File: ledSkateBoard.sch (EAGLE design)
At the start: 25 parts, among them J1 JST, U1 MPU-9150, U2 ATMEGA328P_TQFP, U4 MIC2505 3.3

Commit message: Final on revA
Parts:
- removed R10: 36K, SparkFun-Resistors:RESISTOR0805-RES
- removed R9: 4.3K, SparkFun-Resistors:RESISTOR0805-RES
- removed TP3: TEST-POINT3, SparkFun-Passives:TEST-POINT3
- added C2, C3: 22pF, SparkFun-Capacitors:CAP1206
- added C4: 10uF, SparkFun-Capacitors:CAP1206
- added D2: GREEN, SparkFun-LED:LED-GREENLARGE
- added D3, D4: PMEG4005EJ, SparkFun-DiscreteSemi:DIODE-SCHOTTKY-PMEG4005EJ
- added FB1: (no value), microbuilder:FERRITE0805
- added JP2: (no value), SparkFun-Connectors:M06LOCK
- added Q1: 16Mhz, adafruit:CRYSTALHC49S
- added R1: 330, SparkFun-Passives:RESISTOR1206
- added R2: 37K, SparkFun-Passives:RESISTOR1206
- added R3: 430K, SparkFun-Passives:RESISTOR1206
- added U3: (no value), adafruit:GPS_FGPMMOPA6H
- C1: value 10uF -> 10nF; device SparkFun-Capacitors:CAP0805 -> SparkFun-Capacitors:CAP1206
- C10, C13, C14, C15, C17, C9: device SparkFun-Capacitors:CAP0805 -> SparkFun-Capacitors:CAP1206
- C11: value 4.7uF -> .1uF; device SparkFun-Capacitors:CAP0805 -> SparkFun-Capacitors:CAP1206
- C12: value 4.7uF -> 2.2nF 50V; device SparkFun-Capacitors:CAP0805 -> SparkFun-Capacitors:CAP1206
- D1: device SparkFun-LED:LED-RED0603 -> SparkFun-LED:LED-RED1206
- JP3: value LED CONNECTOR -> M02LOCK; device SparkFun-Connectors:M03PTH -> SparkFun-Connectors:M02LOCK
- R11, R12: value 10K -> 4.7K; device SparkFun-Resistors:RESISTOR0805-RES -> SparkFun-Passives:RESISTOR1206
- R13, R14, R8: device SparkFun-Resistors:RESISTOR0805-RES -> SparkFun-Passives:RESISTOR1206
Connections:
- removed net DATA: JP3.2, U2.PB0(ICP)
- removed net MPU_INT: U1.INT, U2.PD2(INT0)
- new net AN0: JP2.2, U2.PD6(AIN0)
- new net AN1: JP2.3, U2.PD7(AIN1)
- new net GPS_RX: JP3.2, U2.PD1(TXD), U3.RX
- new net GPS_TX: JP3.1, U2.PD0(RXD), U3.TX
- new net N$10: C14.2, D3.C, D4.C, U4.EN, U4.IN
- new net N$3: C2.1, Q1.2, U2.PB6(XTAL1/TOSC1)
- new net N$5: C3.1, Q1.1, U2.PB7(XTAL2/TOSC2)
- new net N$6: D2.A, U3.3D-FIX
- new net N$9: D2.C, R1.1
- new net PB0: JP2.4
- new net PB1: JP2.5, U2.PB1(OC1A)
- new net PB2: JP2.6, U2.PB2(SS/OC1B)
- new net PD5: JP2.1, U2.PD5(T1)
- new net PWR_MNTR: R2.1, R3.2, U2.PC0(ADC0)
- net 5V: now also D3.A, JP1.2
- net GND: now also C2.2, C3.2, C4.2, R1.2, R3.1, U3.GND@1, U3.GND@2, U3.GND@4; no longer JP3.3, R10.1
- net N$4: now also C4.1, FB1.P$1, U3.VCC; no longer R10.2, R9.1, TP3.1, U2.PC0(ADC0)
- net VCC: now also FB1.P$2; no longer JP1.2
- net V_BATT: now also D4.A, R2.2; no longer C14.2, JP3.1, R9.2, U4.EN, U4.IN
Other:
- moved on the sheet: C1, C10, C11, C12, C13, C14, C15, C17, C9, D1, J1, JP1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

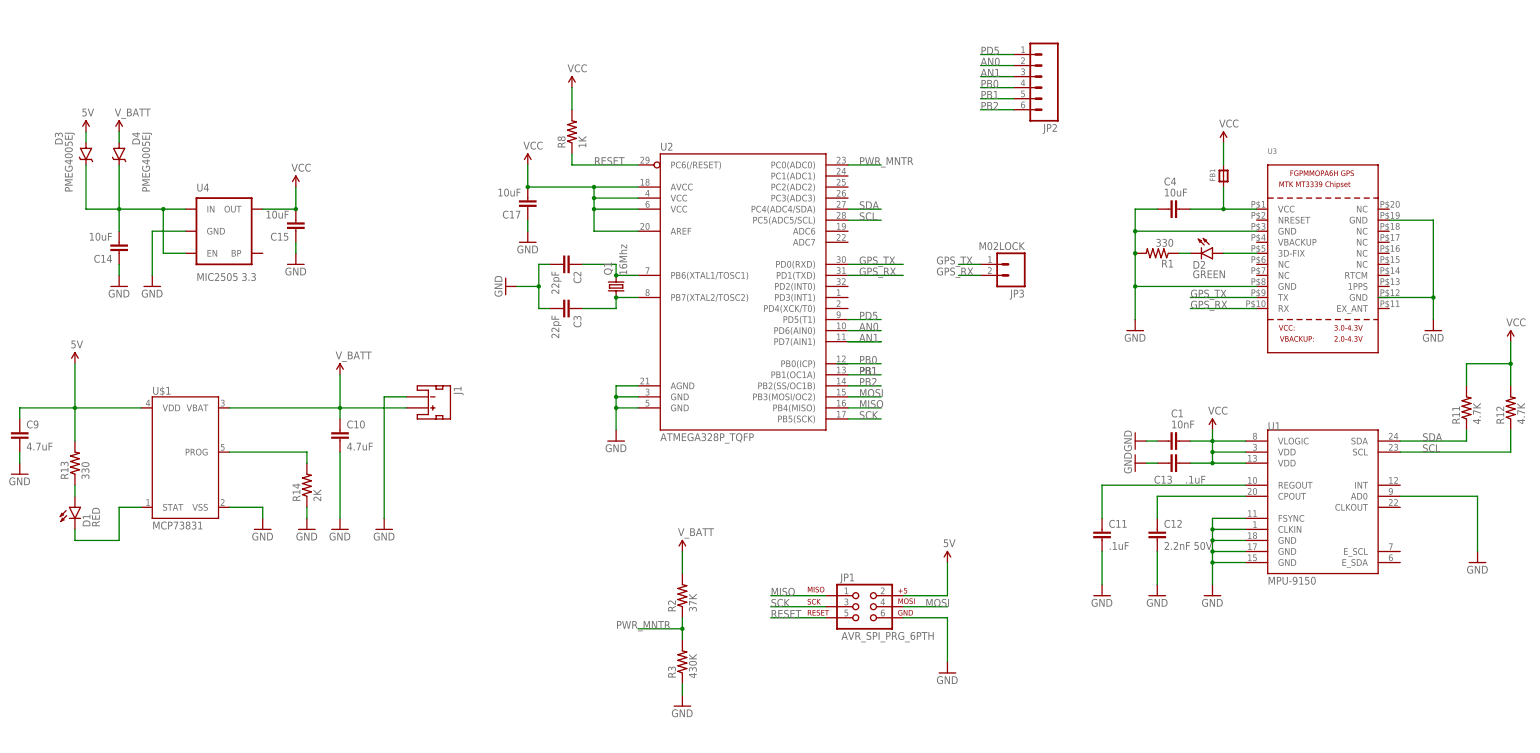
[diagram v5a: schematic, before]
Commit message: Changed to lpc1114 and BNO055
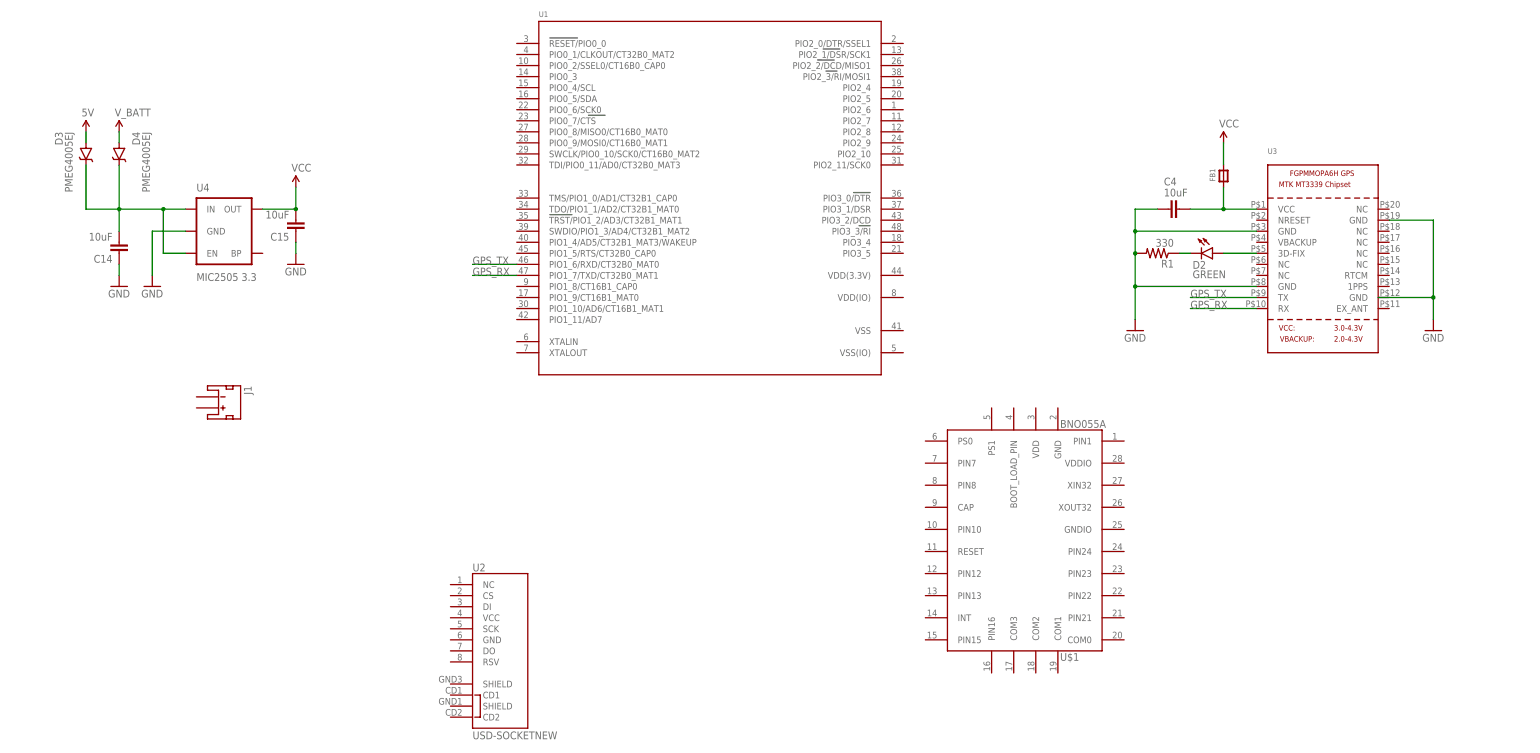
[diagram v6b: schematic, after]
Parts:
- removed C1: 10nF, SparkFun-Capacitors:CAP1206
- removed C10, C9: 4.7uF, SparkFun-Capacitors:CAP1206
- removed C11, C13: .1uF, SparkFun-Capacitors:CAP1206
- removed C12: 2.2nF 50V, SparkFun-Capacitors:CAP1206
- removed C17: 10uF, SparkFun-Capacitors:CAP1206
- removed C2, C3: 22pF, SparkFun-Capacitors:CAP1206
- removed D1: RED, SparkFun-LED:LED-RED1206
- removed JP1: AVR_SPI_PRG_6PTH, SparkFun-Connectors:AVR_SPI_PRG_6PTH
- removed JP2: (no value), SparkFun-Connectors:M06LOCK
- removed JP3: M02LOCK, SparkFun-Connectors:M02LOCK
- removed Q1: 16Mhz, adafruit:CRYSTALHC49S
- removed R11, R12: 4.7K, SparkFun-Passives:RESISTOR1206
- removed R13: 330, SparkFun-Passives:RESISTOR1206
- removed R14: 2K, SparkFun-Passives:RESISTOR1206
- removed R2: 37K, SparkFun-Passives:RESISTOR1206
- removed R3: 430K, SparkFun-Passives:RESISTOR1206
- removed R8: 1K, SparkFun-Passives:RESISTOR1206
- U$1: value MCP73831 -> BNO055A; device GeekAmmo:MCP73831 -> BNO055:BNO055A
- U1: value MPU-9150 -> (none); device SparkFun-Sensors:MPU-9150QFN-24-NP -> microbuilder:LPC1113/4
- U2: value ATMEGA328P_TQFP -> USD-SOCKETNEW; device SparkFun-DigitalIC:ATMEGA328P_TQFP -> SparkFun-Connectors:USD-SOCKETNEW
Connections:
- removed net AN0: JP2.2, U2.PD6(AIN0)
- removed net AN1: JP2.3, U2.PD7(AIN1)
- removed net MISO: JP1.1, U2.PB4(MISO)
- removed net MOSI: JP1.4, U2.PB3(MOSI/OC2)
- removed net N$1: C11.1, U1.REGOUT
- removed net N$11: R14.2, U$1.PROG
- removed net N$2: C12.1, U1.CPOUT
- removed net N$3: C2.1, Q1.2, U2.PB6(XTAL1/TOSC1)
- removed net N$5: C3.1, Q1.1, U2.PB7(XTAL2/TOSC2)
- removed net N$7: D1.A, R13.1
- removed net N$8: D1.C, U$1.STAT
- removed net PB0: JP2.4
- removed net PB1: JP2.5, U2.PB1(OC1A)
- removed net PB2: JP2.6, U2.PB2(SS/OC1B)
- removed net PD5: JP2.1, U2.PD5(T1)
- removed net PWR_MNTR: R2.1, R3.2, U2.PC0(ADC0)
- removed net RESET: JP1.5, R8.1, U2.PC6(/RESET)
- removed net SCK: JP1.3, U2.PB5(SCK)
- removed net SCL: R12.1, U1.SCL, U2.PC5(ADC5/SCL)
- removed net SDA: R11.1, U1.SDA, U2.PC4(ADC4/SDA)
- net 5V: no longer C9.1, JP1.2, R13.2, U$1.VDD
- net GND: no longer C1.1, C10.2, C11.2, C12.2, C13.1, C17.1, C2.2, C3.2, C9.2, J1.-, JP1.6, R14.1, R3.1, U$1.VSS, U1.AD0, U1.CLKIN, U1.FSYNC, U1.GND@15, U1.GND@17, U1.GND@18, U2.AGND, U2.GND@3, U2.GND@5
- net GPS_RX: now also U1.PIO1_7/TXD/CT32B0_MAT1; no longer JP3.2, U2.PD1(TXD)
- net GPS_TX: now also U1.PIO1_6/RXD/CT32B0_MAT0; no longer JP3.1, U2.PD0(RXD)
- net VCC: no longer C1.2, C13.2, C17.2, R11.2, R12.2, R8.2, U1.VDD@13, U1.VDD@3, U1.VLOGIC, U2.AREF, U2.AVCC, U2.VCC@4, U2.VCC@6
- net V_BATT: no longer C10.1, J1.+, R2.2, U$1.VBAT
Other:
- moved on the sheet: J1

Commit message: faileld attempt
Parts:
- removed D3, D4: PMEG4005EJ, SparkFun-DiscreteSemi:DIODE-SCHOTTKY-PMEG4005EJ
- removed U2: USD-SOCKETNEW, SparkFun-Connectors:USD-SOCKETNEW
- removed U3: (no value), adafruit:GPS_FGPMMOPA6H
- added BNO055: BNO055A, BNO055:BNO055A
- added BNO180: BMP180, SparkFun-Sensors:BMP180
- added C2, C3, C6, C7: 10uF, SparkFun-Passives:CAP0805
- added C5: .1uF, SparkFun-Passives:CAP0805
- added D1: PURPLE, SparkFun-LED:LED-PURPLE1206
- added ISP_SWITCH, RST_SWITCH: SWITCH-MOMENTARY-2SMD-1101NE, SparkFun-Electromechanical:SWITCH-MOMENTARY-2SMD-1101NE
- added JP1: (no value), SparkFun-Connectors:M04LOCK
- added MTK339: (no value), adafruit:GPS_FGPMMOPA6H
- added R2, R3, R5, R6: 10K, SparkFun-Passives:RESISTOR0805-RES
- added R4: 330, SparkFun-Passives:RESISTOR0805-RES
- C14, C15, C4: device SparkFun-Capacitors:CAP1206 -> SparkFun-Passives:CAP0805
- R1: device SparkFun-Passives:RESISTOR1206 -> SparkFun-Passives:RESISTOR0805-RES
- U$1: value BNO055A -> MICROSD; device BNO055:BNO055A -> adafruit:MICROSD
- renumbered U1 to LPC1114
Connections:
- removed net 5V: D3.A
- removed net GPS_RX: LPC1114.PIO1_7/TXD/CT32B0_MAT1, U3.RX
- removed net GPS_TX: LPC1114.PIO1_6/RXD/CT32B0_MAT0, U3.TX
- removed net N$10: C14.2, D3.C, D4.C, U4.EN, U4.IN
- new net BNO_INT: BNO055.INT, LPC1114.PIO0_3
- new net ISP: ISP_SWITCH.2, LPC1114.PIO0_1/CLKOUT/CT32B0_MAT2, R5.1
- new net LPC_RX: JP1.2, LPC1114.PIO1_6/RXD/CT32B0_MAT0, MTK339.TX
- new net LPC_TX: JP1.3, LPC1114.PIO1_7/TXD/CT32B0_MAT1, MTK339.RX
- new net N$1: D1.A, LPC1114.PIO2_6
- new net N$2: BNO055.CAP, C2.2
- new net N$3: D1.C, R4.2
- new net RESET: LPC1114.RESET/PIO0_0, R6.1, RST_SWITCH.2
- new net SCL: BNO055.COM1, BNO180.SCL, LPC1114.PIO0_4/SCL, R3.2
- new net SDA: BNO055.COM0, BNO180.SDA, LPC1114.PIO0_5/SDA, R2.2
- new net SD_CS: LPC1114.PIO0_2/SSEL0/CT16B0_CAP0, U$1.CS
- new net SD_DETECT: U$1.CARD_DETECT
- new net SD_DI: LPC1114.PIO0_9/MOSI0/CT16B0_MAT1, U$1.DATA_IN
- new net SD_DO: LPC1114.PIO0_8/MISO0/CT16B0_MAT0, U$1.DATA_OUT
- new net SD_SCK: LPC1114.PIO0_6/SCK0, U$1.SCLK
- new net VDD: U$1.VDD
- new net VSS: U$1.VSS
- net GND: now also BNO055.COM2, BNO055.COM3, BNO055.GND, BNO055.GNDIO, BNO055.PIN10, BNO055.PIN15, BNO055.PIN16, BNO055.PS0, BNO055.PS1, BNO180.GND, C2.1, C3.2, C5.1, C6.2, C7.2, ISP_SWITCH.1, J1.-, JP1.4, LPC1114.VSS, LPC1114.VSS(IO), MTK339.GND@1, MTK339.GND@2, MTK339.GND@3, MTK339.GND@4, R4.1, RST_SWITCH.1, U$1.GND, U$1.GND1; no longer U3.GND@1, U3.GND@2, U3.GND@4
- net N$4: now also MTK339.VCC; no longer U3.VCC
- net N$6: now also MTK339.3D-FIX; no longer U3.3D-FIX
- net VCC: now also BNO055.BOOT_LOAD_PIN, BNO055.RESET, BNO055.VDD, BNO055.VDDIO, BNO180.VDD, BNO180.VDDIO, C3.1, C5.2, C6.1, C7.1, JP1.1, LPC1114.VDD(3.3V), LPC1114.VDD(IO), R2.1, R3.1, R5.2, R6.2
- net V_BATT: now also C14.2, J1.+, U4.EN, U4.IN; no longer D4.A
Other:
- moved on the sheet: C14, C15, C4, D2, FB1, J1, R1, U4

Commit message: semi final version pending review
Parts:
- removed C6: 10uF, SparkFun-Passives:CAP0805
- removed LPC1114: (no value), microbuilder:LPC1113/4
- removed R2, R3: 10K, SparkFun-Passives:RESISTOR0805-RES
- removed U$1: MICROSD, adafruit:MICROSD
- added C1, C8: 10uF, SparkFun-Passives:CAP0805
- added R7, R8: 10K, SparkFun-Passives:RESISTOR0805-RES
- added SDCARD: MICROSD, adafruit:MICROSD
- added U1: (no value), microbuilder:LPC1113/4_QFP_SQUARE
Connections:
- removed net VDD: U$1.VDD
- removed net VSS: U$1.VSS
- new net N$5: R8.2, U1.PIO0_5/SDA
- new net N$7: R4.1
- new net N$8: R7.2, U1.PIO0_4/SCL
- net BNO_INT: now also U1.PIO2_5; no longer LPC1114.PIO0_3
- net GND: now also C1.2, C3.1, C8.2, SDCARD.GND, SDCARD.GND1, SDCARD.VSS, U1.VSS, U1.VSS(IO); no longer C3.2, C6.2, LPC1114.VSS, LPC1114.VSS(IO), R4.1, U$1.GND, U$1.GND1
- net ISP: now also U1.PIO0_1/CLKOUT/CT32B0_MAT2; no longer LPC1114.PIO0_1/CLKOUT/CT32B0_MAT2
- net LPC_RX: now also U1.PIO1_6/RXD/CT32B0_MAT0; no longer LPC1114.PIO1_6/RXD/CT32B0_MAT0
- net LPC_TX: now also U1.PIO1_7/TXD/CT32B0_MAT1; no longer LPC1114.PIO1_7/TXD/CT32B0_MAT1
- net N$1: now also U1.PIO3_0/DTR; no longer LPC1114.PIO2_6
- net RESET: now also U1.RESET/PIO0_0; no longer LPC1114.RESET/PIO0_0
- net SCL: no longer LPC1114.PIO0_4/SCL, R3.2
- net SDA: no longer LPC1114.PIO0_5/SDA, R2.2
- net SD_CS: now also SDCARD.CS, U1.PIO0_2/SSEL0/CT16B0_CAP0; no longer LPC1114.PIO0_2/SSEL0/CT16B0_CAP0, U$1.CS
- net SD_DETECT: now also SDCARD.CARD_DETECT; no longer U$1.CARD_DETECT
- net SD_DI: now also SDCARD.DATA_IN, U1.PIO0_9/MOSI0/CT16B0_MAT1; no longer LPC1114.PIO0_9/MOSI0/CT16B0_MAT1, U$1.DATA_IN
- net SD_DO: now also SDCARD.DATA_OUT, U1.PIO0_8/MISO0/CT16B0_MAT0; no longer LPC1114.PIO0_8/MISO0/CT16B0_MAT0, U$1.DATA_OUT
- net SD_SCK: now also SDCARD.SCLK, U1.PIO0_6/SCK0; no longer LPC1114.PIO0_6/SCK0, U$1.SCLK
- net VCC: now also C1.1, C3.2, C8.1, R7.1, R8.1, SDCARD.VDD, U1.VDD(3.3V), U1.VDD(IO); no longer C3.1, C6.1, LPC1114.VDD(3.3V), LPC1114.VDD(IO), R2.1, R3.1
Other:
- moved on the sheet: BNO055, BNO180, C14, C15, C2, C3, C4, C5, C7, D1, D2, FB1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
